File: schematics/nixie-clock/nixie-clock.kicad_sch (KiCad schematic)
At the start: 68 parts, among them J1 Barrel_Jack_Switch, J2 Conn_02x03_Odd_Even, J3 Conn_01x04, J4 Conn_01x07, J5 Conn_01x07, J6 Screw_Terminal_01x02, J7 Screw_Terminal_01x02, Q1 MJE13007, Q2 MJE13007, SW1 SW_Push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

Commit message: pcb: finished, tweaks to be done
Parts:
- R11, R12, R13, R14, R15, R16, R17, R18: footprint Resistor_THT:R_Axial_DIN0309_L9.0mm_D3.2mm_P12.70mm_Horizontal -> Resistor_SMD:R_1206_3216Metric_Pad1.30x1.75mm_HandSolder
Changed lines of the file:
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@@
       (effects (font (size 1.27 1.27)) (justify left))
     )
-    (property "Footprint" "Resistor_THT:R_Axial_DIN0309_L9.0mm_D3.2mm_P12.70mm_Horizontal" (id 2) (at 278.13 53.848 90)
+    (property "Footprint" "Resistor_SMD:R_1206_3216Metric_Pad1.30x1.75mm_HandSolder" (id 2) (at 278.13 53.848 90)
       (effects (font (size 1.27 1.27)) hide)
     )
@@
       (effects (font (size 1.27 1.27)) (justify left))
     )
-    (property "Footprint" "Resistor_THT:R_Axial_DIN0309_L9.0mm_D3.2mm_P12.70mm_Horizontal" (id 2) (at 381 112.268 90)
+    (property "Footprint" "Resistor_SMD:R_1206_3216Metric_Pad1.30x1.75mm_HandSolder" (id 2) (at 381 112.268 90)
       (effects (font (size 1.27 1.27)) hide)
     )
@@
       (effects (font (size 1.27 1.27)) (justify left))
     )
-    (property "Footprint" "Resistor_THT:R_Axial_DIN0309_L9.0mm_D3.2mm_P12.70mm_Horizontal" (id 2) (at 381 53.848 90)
+    (property "Footprint" "Resistor_SMD:R_1206_3216Metric_Pad1.30x1.75mm_HandSolder" (id 2) (at 381 53.848 90)
       (effects (font (size 1.27 1.27)) hide)
     )
@@
       (effects (font (size 1.27 1.27)) (justify left))
     )
-    (property "Footprint" "Resistor_THT:R_Axial_DIN0309_L9.0mm_D3.2mm_P12.70mm_Horizontal" (id 2) (at 381 109.728 90)
+    (property "Footprint" "Resistor_SMD:R_1206_3216Metric_Pad1.30x1.75mm_HandSolder" (id 2) (at 381 109.728 90)
       (effects (font (size 1.27 1.27)) hide)
     )
@@
       (effects (font (size 1.27 1.27)) (justify left))
     )
-    (property "Footprint" "Resistor_THT:R_Axial_DIN0309_L9.0mm_D3.2mm_P12.70mm_Horizontal" (id 2) (at 278.13 112.268 90)
+    (property "Footprint" "Resistor_SMD:R_1206_3216Metric_Pad1.30x1.75mm_HandSolder" (id 2) (at 278.13 112.268 90)
       (effects (font (size 1.27 1.27)) hide)
     )
@@
       (effects (font (size 1.27 1.27)) (justify left))
     )
-    (property "Footprint" "Resistor_THT:R_Axial_DIN0309_L9.0mm_D3.2mm_P12.70mm_Horizontal" (id 2) (at 381 56.388 90)
+    (property "Footprint" "Resistor_SMD:R_1206_3216Metric_Pad1.30x1.75mm_HandSolder" (id 2) (at 381 56.388 90)
       (effects (font (size 1.27 1.27)) hide)
     )
@@
       (effects (font (size 1.27 1.27)) (justify left))
     )
-    (property "Footprint" "Resistor_THT:R_Axial_DIN0309_L9.0mm_D3.2mm_P12.70mm_Horizontal" (id 2) (at 278.13 109.728 90)
+    (property "Footprint" "Resistor_SMD:R_1206_3216Metric_Pad1.30x1.75mm_HandSolder" (id 2) (at 278.13 109.728 90)
       (effects (font (size 1.27 1.27)) hide)
     )
@@
       (effects (font (size 1.27 1.27)) (justify left))
     )
-    (property "Footprint" "Resistor_THT:R_Axial_DIN0309_L9.0mm_D3.2mm_P12.70mm_Horizontal" (id 2) (at 278.13 56.388 90)
+    (property "Footprint" "Resistor_SMD:R_1206_3216Metric_Pad1.30x1.75mm_HandSolder" (id 2) (at 278.13 56.388 90)
       (effects (font (size 1.27 1.27)) hide)
     )
@@
     )
     (path "/33878cb0-de93-49ba-844f-9667b0ba12b2"
-      (reference "R11") (unit 1) (value "33k") (footprint "Resistor_THT:R_Axial_DIN0309_L9.0mm_D3.2mm_P12.70mm_Horizontal")
+      (reference "R11") (unit 1) (value "33k") (footprint "Resistor_SMD:R_1206_3216Metric_Pad1.30x1.75mm_HandSolder")
     )
     (path "/e7cc63fe-687a-4121-9439-ff9d1ac38731"
-      (reference "R12") (unit 1) (value "33k") (footprint "Resistor_THT:R_Axial_DIN0309_L9.0mm_D3.2mm_P12.70mm_Horizontal")
+      (reference "R12") (unit 1) (value "33k") (footprint "Resistor_SMD:R_1206_3216Metric_Pad1.30x1.75mm_HandSolder")
     )
     (path "/e7265a88-68e8-40b6-b2eb-0f4f50ca20da"
-      (reference "R13") (unit 1) (value "33k") (footprint "Resistor_THT:R_Axial_DIN0309_L9.0mm_D3.2mm_P12.70mm_Horizontal")
+      (reference "R13") (unit 1) (value "33k") (footprint "Resistor_SMD:R_1206_3216Metric_Pad1.30x1.75mm_HandSolder")
     )
     (path "/8de68870-5d02-4792-905b-2e9e44982a07"
-      (reference "R14") (unit 1) (value "33k") (footprint "Resistor_THT:R_Axial_DIN0309_L9.0mm_D3.2mm_P12.70mm_Horizontal")
+      (reference "R14") (unit 1) (value "33k") (footprint "Resistor_SMD:R_1206_3216Metric_Pad1.30x1.75mm_HandSolder")
     )
     (path "/5fb0dcb2-943c-420c-aebd-d9666bec9461"
-      (reference "R15") (unit 1) (value "33k") (footprint "Resistor_THT:R_Axial_DIN0309_L9.0mm_D3.2mm_P12.70mm_Horizontal")
+      (reference "R15") (unit 1) (value "33k") (footprint "Resistor_SMD:R_1206_3216Metric_Pad1.30x1.75mm_HandSolder")
     )
     (path "/e1dc4706-0183-473b-81c7-6e41bda8539b"
-      (reference "R16") (unit 1) (value "33k") (footprint "Resistor_THT:R_Axial_DIN0309_L9.0mm_D3.2mm_P12.70mm_Horizontal")
+      (reference "R16") (unit 1) (value "33k") (footprint "Resistor_SMD:R_1206_3216Metric_Pad1.30x1.75mm_HandSolder")
     )
     (path "/7f6fb953-b879-4cf3-899d-d9c1f19ff760"
-      (reference "R17") (unit 1) (value "33k") (footprint "Resistor_THT:R_Axial_DIN0309_L9.0mm_D3.2mm_P12.70mm_Horizontal")
+      (reference "R17") (unit 1) (value "33k") (footprint "Resistor_SMD:R_1206_3216Metric_Pad1.30x1.75mm_HandSolder")
     )
     (path "/51b308d9-297a-4c56-aef8-c907eba6b96c"
-      (reference "R18") (unit 1) (value "33k") (footprint "Resistor_THT:R_Axial_DIN0309_L9.0mm_D3.2mm_P12.70mm_Horizontal")
+      (reference "R18") (unit 1) (value "33k") (footprint "Resistor_SMD:R_1206_3216Metric_Pad1.30x1.75mm_HandSolder")
     )
     (path "/9799c809-996d-4dbf-a404-a1e9d0a1cac8"

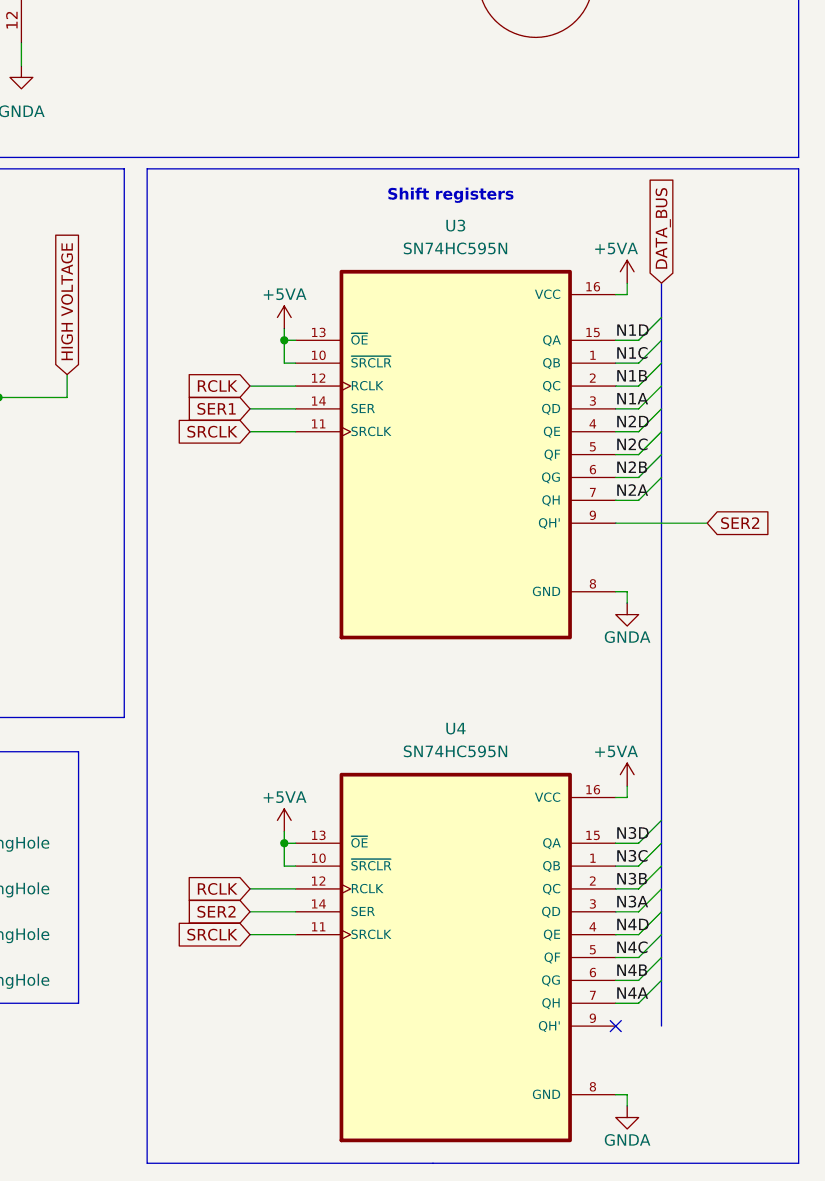
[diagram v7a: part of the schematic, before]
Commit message: schematic correction: active low OE on shift regs is now connected correctly; added pullup and pulldown resistors to shift reg
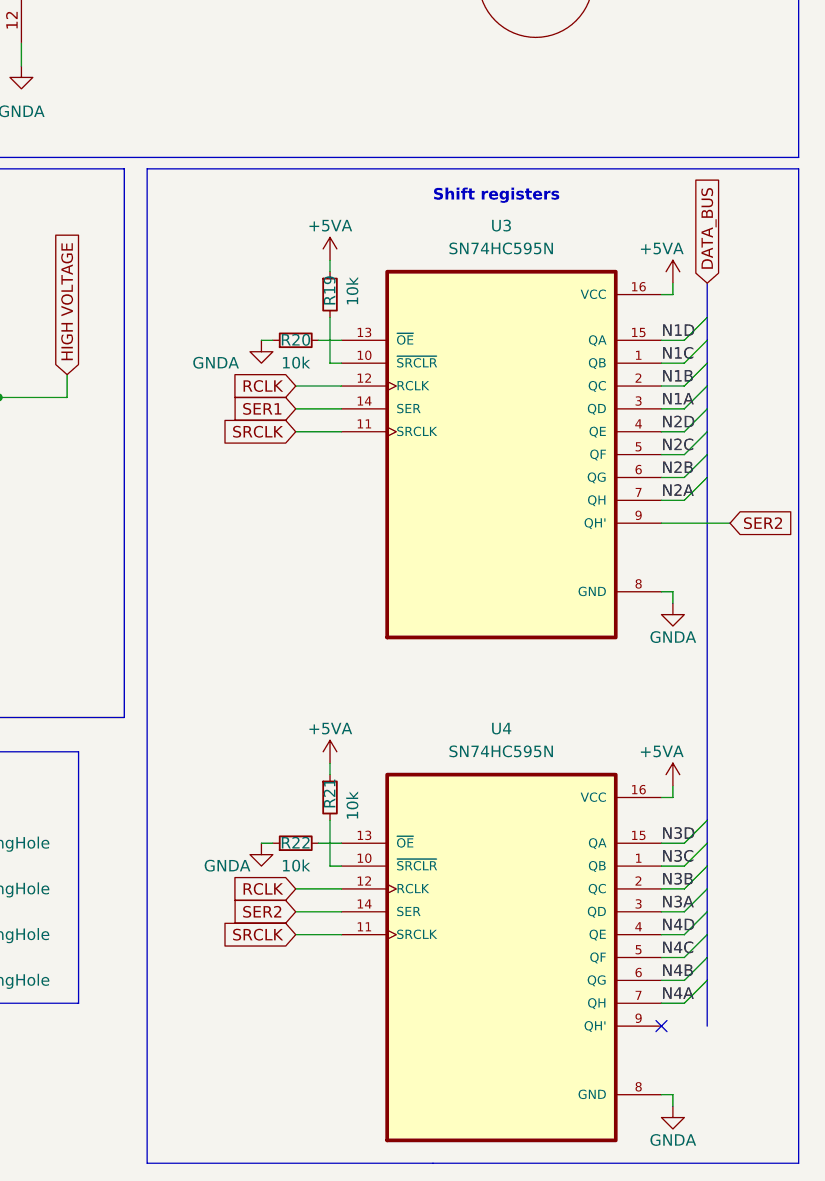
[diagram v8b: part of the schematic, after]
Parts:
- added R19, R20, R21, R22: 10k, Resistor_SMD:R_0805_2012Metric_Pad1.20x1.40mm_HandSolder, symbol Device:R_Small
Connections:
- net +5VA: now also R19.1, R21.1; no longer U3.10 (~{SRCLR}), U3.13 (~{OE}), U4.10 (~{SRCLR}), U4.13 (~{OE})
- net GNDA: now also R20.1, R22.1
- new net: R22.2, U4.13 (~{OE})
- new net: R19.2, U3.10 (~{SRCLR})
- new net: R20.2, U3.13 (~{OE})
- new net: R21.2, U4.10 (~{SRCLR})
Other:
- moved on the sheet: U3, U4
